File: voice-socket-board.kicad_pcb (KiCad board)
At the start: 2 copper layers, 150 x 100 mm, 280 parts, among them J1 JACK_MONO_SW, J2 JACK_MONO_SW, J3 JACK_MONO_SW, P1 CONN_01X03, P2 CONN_01X03, P3 CONN_02X05, P4 DDR3-DIMM, Q1 MMBT3904, Q10 2N3906, Q2 DMMT3904W, Q3 2N7002, Q4 2N7002, Q5 MMBT3904, Q6 2N3906, Q7 MMBT3904, Q8 MMBT3904, Q9 MMBT3904, SW1 SPST, SW10 SP3T, SW11 SP3T, SW12 SP3T, SW13 SP3T, SW14 SPST, SW15 TACT_SWITCH, SW2 SPST, SW3 SP3T, SW4 SP3T, SW5 SPST, SW6 SPST, SW7 Switch_SPDT_x2, SW8 2P3T, SW9 SP3T, U1 LM833, U10 TL072-, U11 NE5534, U2 TL072-, U3 TL072-, U4 TL072-, U5 TL072-, U6 TL072-, U7 MAX9945, U8 CD4013, U9 TL072-

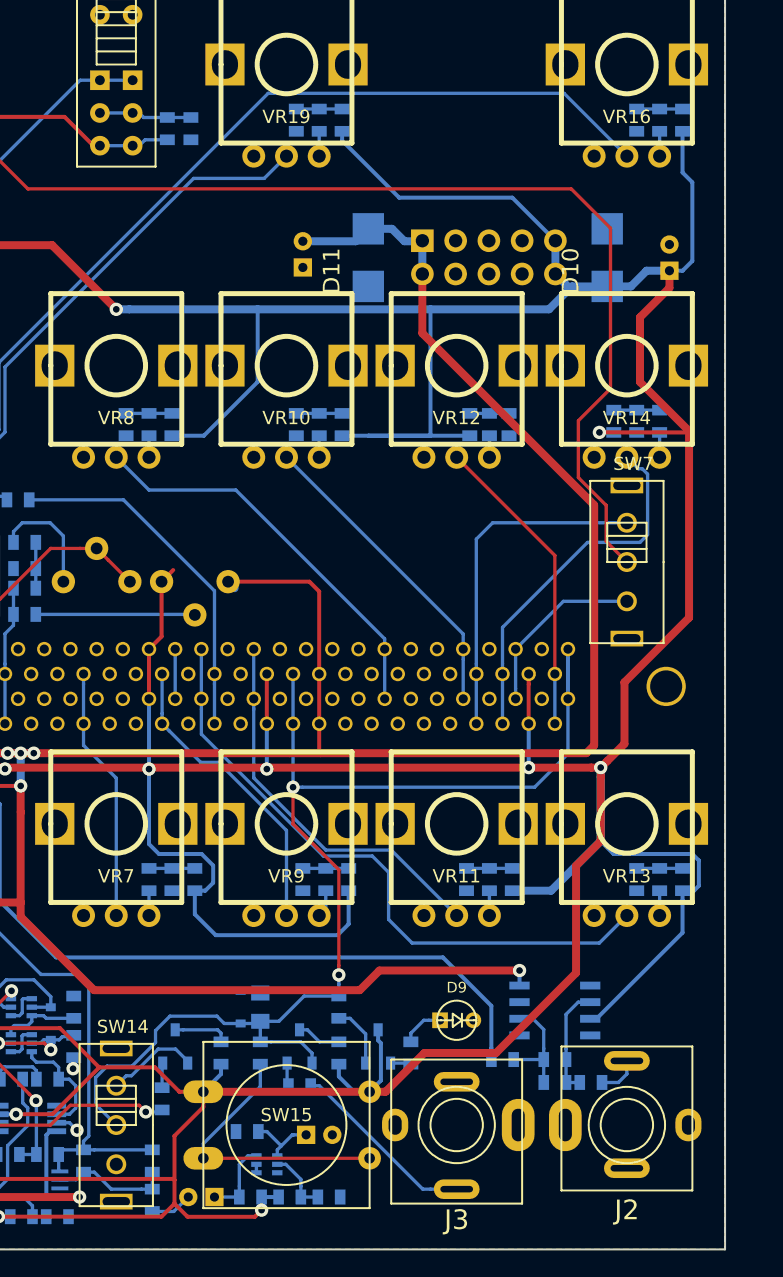
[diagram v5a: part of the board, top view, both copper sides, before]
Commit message: all footprints have proper 3D models associated with them in VRML2.0 format. Still need models for test points
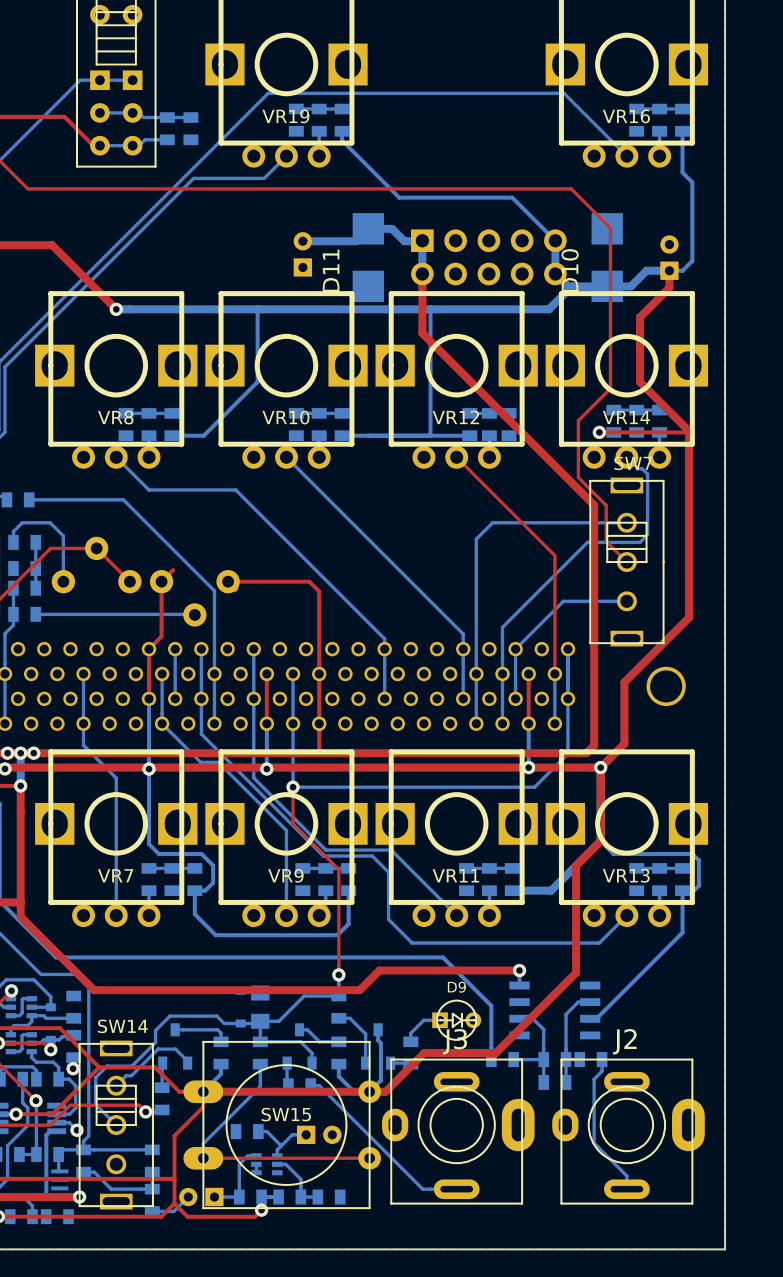
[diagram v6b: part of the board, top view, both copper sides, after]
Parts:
- moved R123 1.75 mm to (184.8, 125.5)
- turned J2 to 180 degrees
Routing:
- net Net-(J2-Pad3): track 3.17 -> 11.2 mm
- net Net-(J2-Pad2): track 0.00 -> 0.91 mm
- net Net-(R98-Pad2): track 52.1 -> 51.6 mm

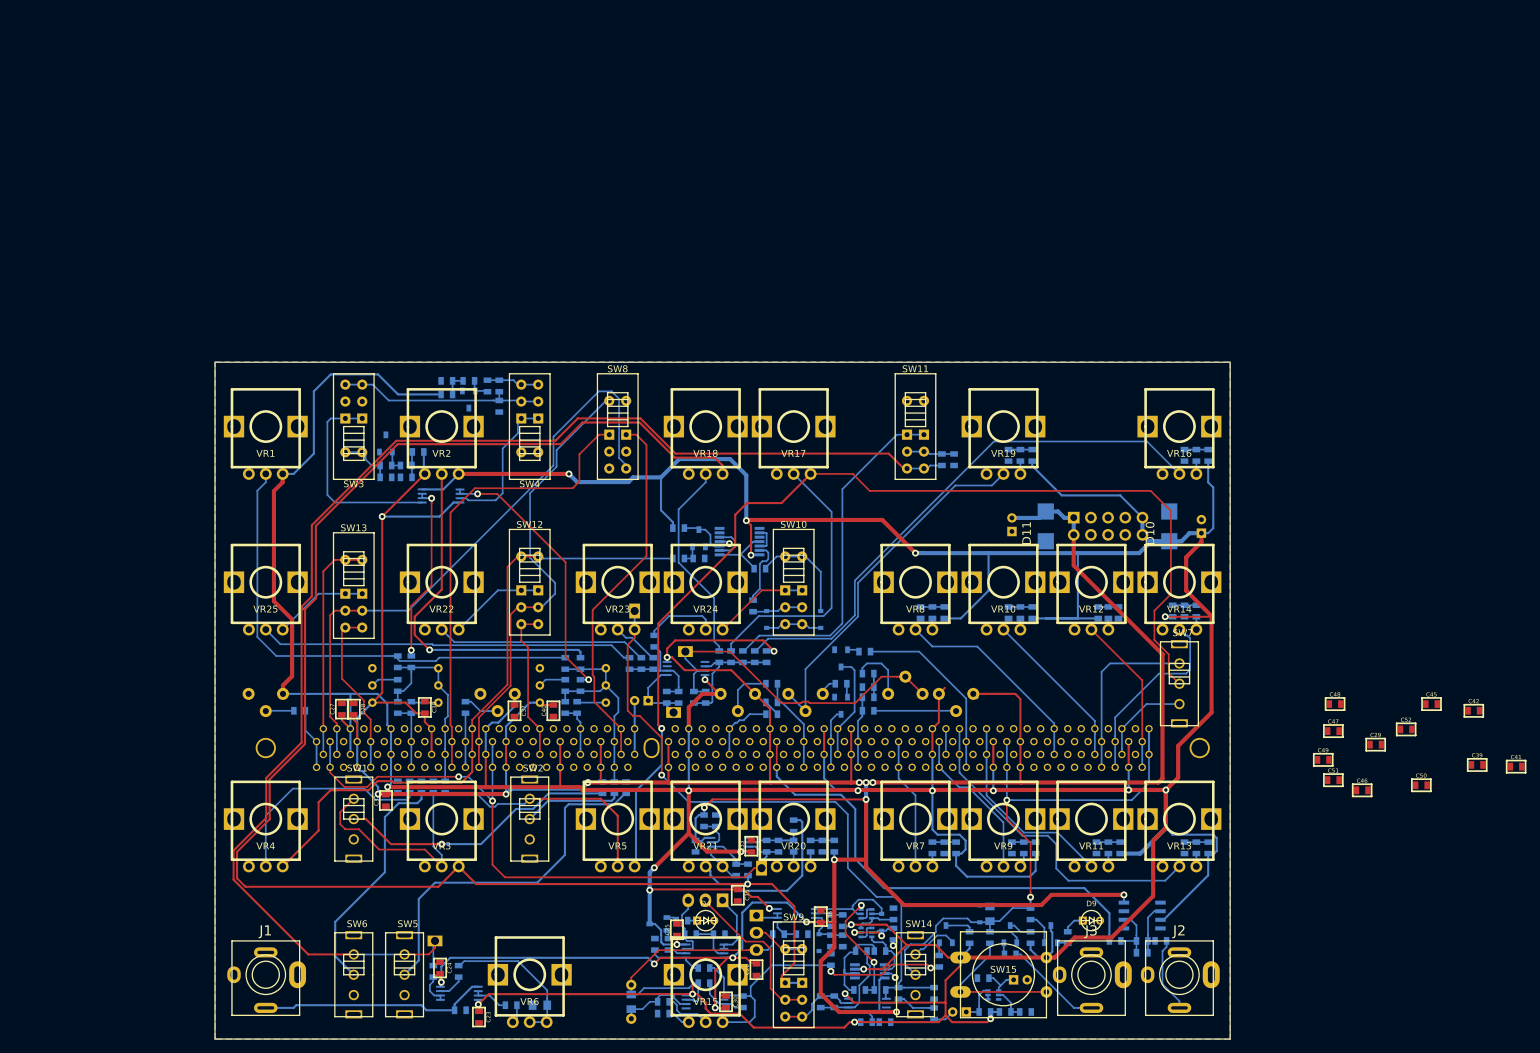
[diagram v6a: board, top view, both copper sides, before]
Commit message: routed. maybe need more decoupling caps
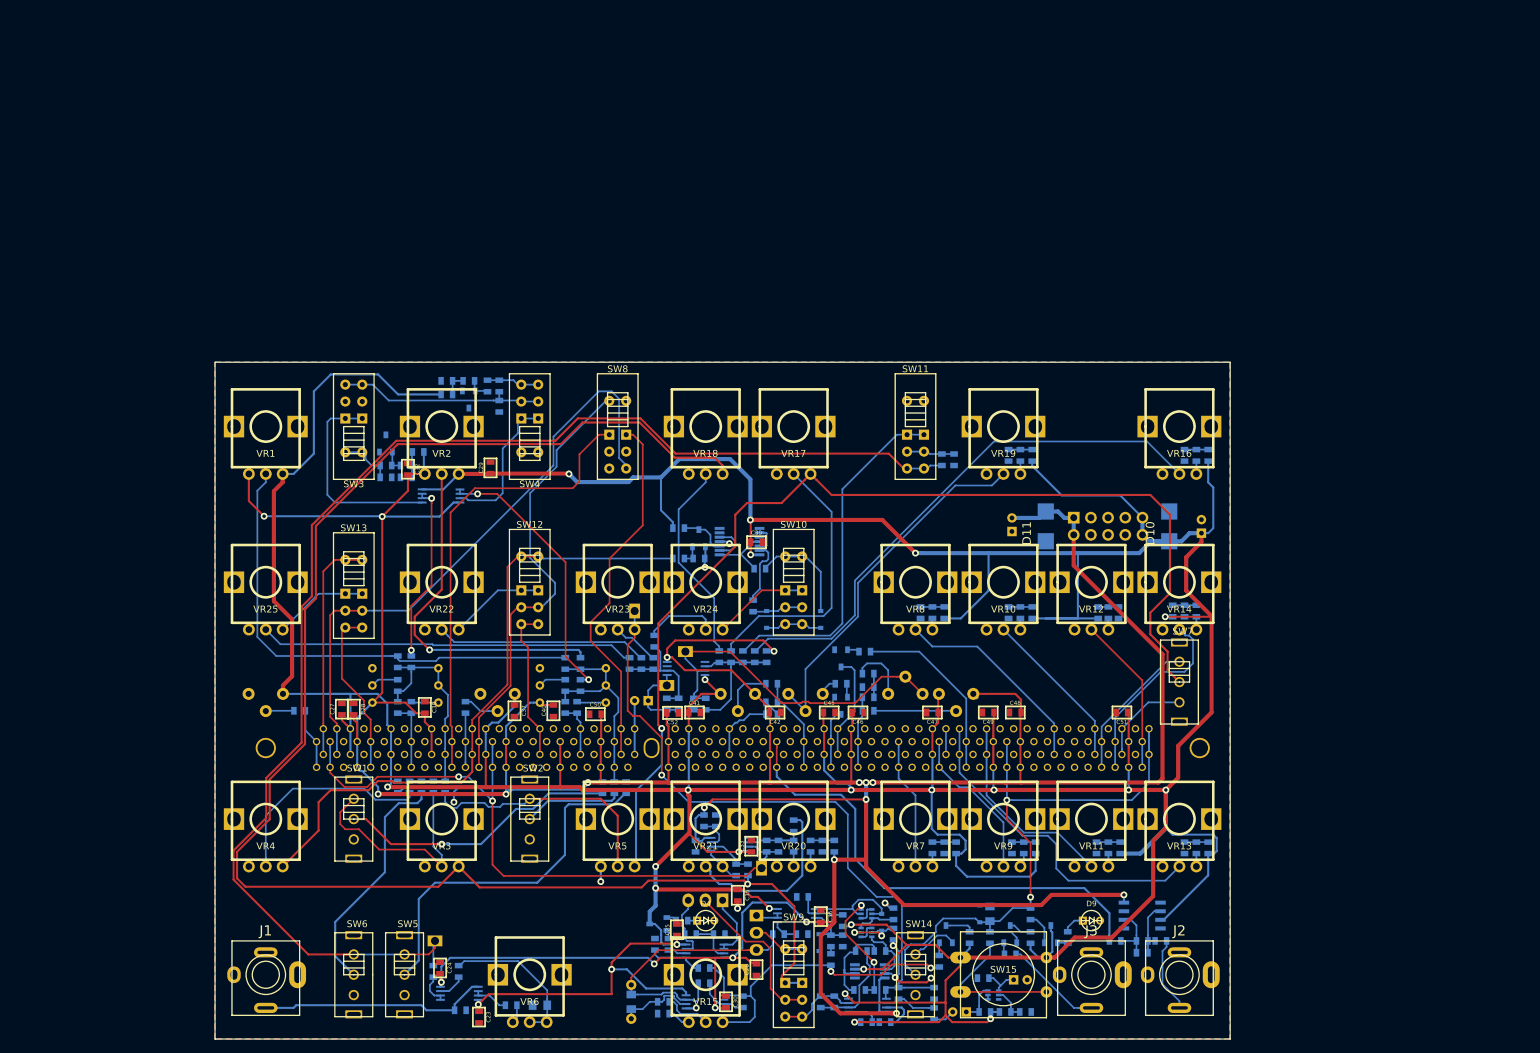
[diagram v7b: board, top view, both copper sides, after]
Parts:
- moved C29 137.0 mm to (85.7, 55.6), turned to 90 degrees
- moved C50 122.5 mm to (101.2, 92.0)
- moved C41 121.7 mm to (115.8, 91.8)
- moved C39 111.5 mm to (125.0, 66.6)
- moved C52 108.4 mm to (112.6, 91.8), turned to 180 degrees
- moved C42 103.3 mm to (127.8, 91.8), turned to 180 degrees
- moved C45 89.0 mm to (135.8, 91.8)
- moved C46 75.4 mm to (140.0, 91.8), turned to 180 degrees
- moved C47 59.3 mm to (151.0, 91.8), turned to 180 degrees
- moved C49 50.0 mm to (159.2, 91.8), turned to 180 degrees
- moved C32 49.1 mm to (73.5, 55.8), turned to 270 degrees
- moved C48 47.3 mm to (163.2, 91.8)
- moved C51 32.8 mm to (179.0, 91.8), turned to 180 degrees
- moved R57 5.47 mm to (131.8, 119.0), turned to 180 degrees
- moved TP5 4.12 mm to (111.8, 87.8)
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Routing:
- net VCO1_PULSE: track 27.6 -> 91.3 mm
- net VCO1_SYNC_IN: track 117.1 -> 67.8 mm
- net GND: track 4.23 -> 42.9 mm, vias 3 -> 10
- net -12V: track 594.4 -> 632.8 mm, vias 19 -> 20
- net VCO2_SYNC_IN: track 68.3 -> 53.9 mm
- net EG2_INV_OUT: track 26.1 -> 21.5 mm
- net +12V: track 927.9 -> 923.8 mm
- net Net-(R56-Pad1): track 4.15 -> 7.54 mm
- net Net-(C57-Pad1): track 18.6 -> 21.1 mm
- net Net-(C14-Pad2): track 41.9 -> 40.2 mm
- net EG2_ENV_MOD: track 35.4 -> 36.8 mm
- net Net-(C57-Pad2): track 50.7 -> 51.7 mm
- net Net-(C59-Pad2): track 16.0 -> 17.0 mm
- net LFO_OUT: track 230.6 -> 231.4 mm
- net Net-(C59-Pad1): track 11.9 -> 12.6 mm
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
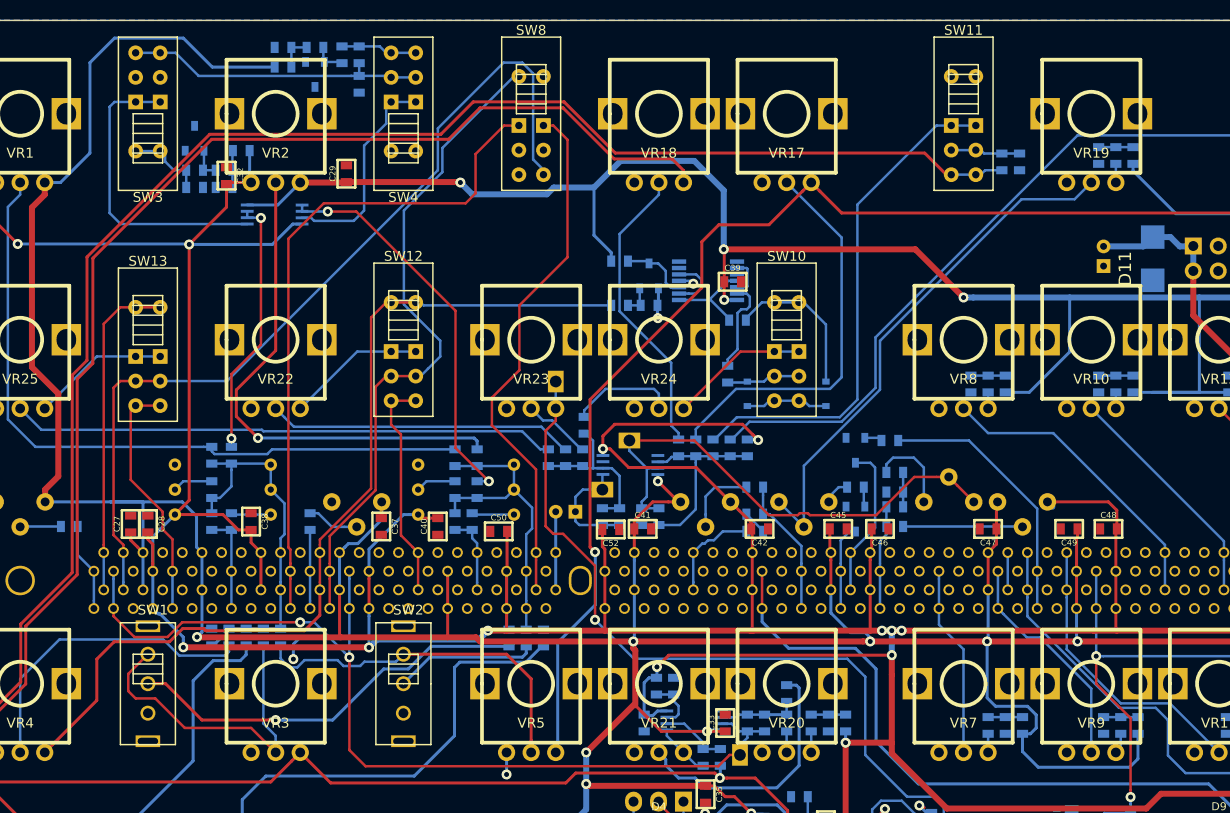
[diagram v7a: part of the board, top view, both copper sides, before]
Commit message: tweaking routing for better ground plane coverage
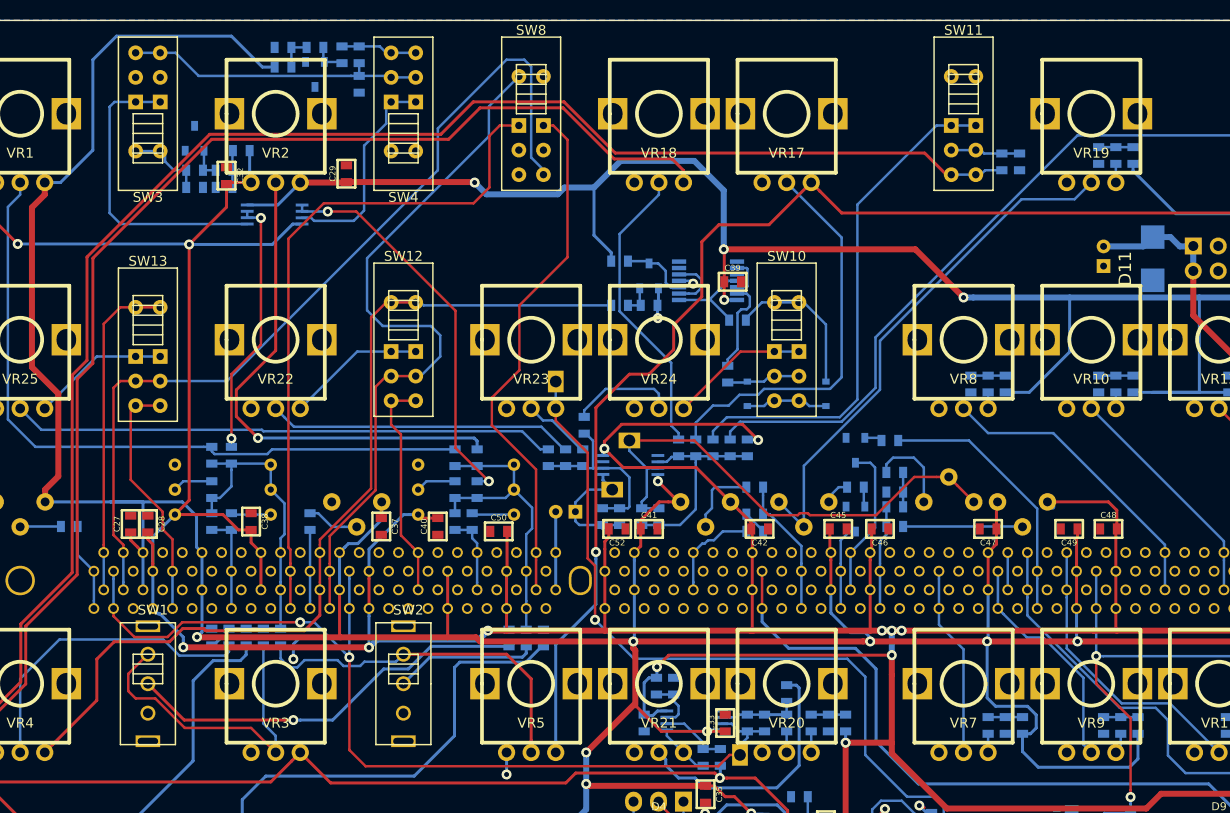
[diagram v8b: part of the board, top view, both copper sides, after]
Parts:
- moved TP5 1.00 mm to (112.8, 87.8)
- moved C52 0.65 mm to (113.2, 91.8)
- moved C41 0.65 mm to (116.5, 91.8)
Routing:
- net VCO2_PULSE: track 67.0 -> 73.2 mm
- net Net-(C59-Pad2): track 17.0 -> 18.8 mm
- net NOISE: track 96.7 -> 95.3 mm
- net Net-(C59-Pad1): track 12.6 -> 13.8 mm
- net VCO1_SYNC_IN: track 67.8 -> 68.5 mm
- net EG2_OUT: track 155.5 -> 156.2 mm
- net VCO1_PULSE: track 91.3 -> 91.8 mm
